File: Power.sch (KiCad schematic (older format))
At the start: 13 parts, among them P1 24 Pin MiniFit JR, SW1 Power Switch

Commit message: Layout Work Session 5
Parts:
- added TP1: CONN_1, symbol CONN_1
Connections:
- net GND: now also TP1.1
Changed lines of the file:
@@
-EESchema Schematic File Version 2  date 11/7/2013 10:50:27 PM
+EESchema Schematic File Version 2  date 11/9/2013 9:10:12 PM
 LIBS:power
 LIBS:device
@@
 Sheet 9 9
 Title ""
-Date "8 nov 2013"
+Date "10 nov 2013"
 Rev ""
 Comp ""
@@
 $EndComp
 $Comp
-L GND #PWR048
+L GND #PWR045
 U 1 1 523DFA76
 P 1400 1850
-F 0 "#PWR048" H 1400 1850 30  0001 C CNN
+F 0 "#PWR045" H 1400 1850 30  0001 C CNN
 F 1 "GND" H 1400 1780 30  0001 C CNN
 F 2 "" H 1400 1850 60  0000 C CNN
@@
 	5500 1900 5500 1150
 $Comp
-L +12P #PWR049
+L +12P #PWR046
 U 1 1 523DFB91
 P 5500 1150
-F 0 "#PWR049" H 5500 1120 30  0001 C CNN
+F 0 "#PWR046" H 5500 1120 30  0001 C CNN
 F 1 "+12P" H 5500 1250 30  0000 C CNN
 F 2 "" H 5500 1150 60  0000 C CNN
@@
 $EndComp
 $Comp
-L -12P #PWR050
+L -12P #PWR047
 U 1 1 523E04D8
 P 6100 1150
-F 0 "#PWR050" H 6100 1280 20  0001 C CNN
+F 0 "#PWR047" H 6100 1280 20  0001 C CNN
 F 1 "-12P" H 6100 1250 30  0000 C CNN
 F 2 "" H 6100 1150 60  0000 C CNN
@@
 	4800 3200 4800 3450
 $Comp
-L GND #PWR051
+L GND #PWR048
 U 1 1 523E08C4
 P 4800 3450
-F 0 "#PWR051" H 4800 3450 30  0001 C CNN
+F 0 "#PWR048" H 4800 3450 30  0001 C CNN
 F 1 "GND" H 4800 3380 30  0001 C CNN
 F 2 "" H 4800 3450 60  0000 C CNN
@@
 	5650 3000 5650 2750
 $Comp
-L +3.3V #PWR052
+L +3.3V #PWR049
 U 1 1 523E0910
 P 5650 2750
-F 0 "#PWR052" H 5650 2710 30  0001 C CNN
+F 0 "#PWR049" H 5650 2710 30  0001 C CNN
 F 1 "+3.3V" H 5650 2860 30  0000 C CNN
 F 2 "" H 5650 2750 60  0000 C CNN
@@
 $EndComp
 $Comp
-L +12P #PWR053
+L +12P #PWR050
 U 1 1 523E0C76
 P 8000 2250
-F 0 "#PWR053" H 8000 2220 30  0001 C CNN
+F 0 "#PWR050" H 8000 2220 30  0001 C CNN
 F 1 "+12P" H 8000 2350 30  0000 C CNN
 F 2 "" H 8000 2250 60  0000 C CNN
@@
 $EndComp
 $Comp
-L -12P #PWR054
+L -12P #PWR051
 U 1 1 523E0C7C
 P 8000 3800
-F 0 "#PWR054" H 8000 3930 20  0001 C CNN
+F 0 "#PWR051" H 8000 3930 20  0001 C CNN
 F 1 "-12P" H 8000 3900 30  0000 C CNN
 F 2 "" H 8000 3800 60  0000 C CNN
@@
 $EndComp
 $Comp
-L GND #PWR055
+L GND #PWR052
 U 1 1 523E0C82
 P 9000 3200
-F 0 "#PWR055" H 9000 3200 30  0001 C CNN
+F 0 "#PWR052" H 9000 3200 30  0001 C CNN
 F 1 "GND" H 9000 3130 30  0001 C CNN
 F 2 "" H 9000 3200 60  0000 C CNN
@@
 Connection ~ 9450 3050
 $Comp
-L -12V #PWR056
+L -12V #PWR053
 U 1 1 523E0DD3
 P 10350 3800
-F 0 "#PWR056" H 10350 3930 20  0001 C CNN
+F 0 "#PWR053" H 10350 3930 20  0001 C CNN
 F 1 "-12V" H 10350 3900 30  0000 C CNN
 F 2 "" H 10350 3800 60  0000 C CNN
@@
 Connection ~ 9450 2450
 $Comp
-L +12V #PWR057
+L +12V #PWR054
 U 1 1 523E0E37
 P 10350 2200
-F 0 "#PWR057" H 10350 2150 20  0001 C CNN
+F 0 "#PWR054" H 10350 2150 20  0001 C CNN
 F 1 "+12V" H 10350 2300 30  0000 C CNN
 F 2 "" H 10350 2200 60  0000 C CNN
@@
 Connection ~ 3450 1900
 $Comp
-L +12C #PWR058
+L +12C #PWR055
 U 1 1 52438F0D
 P 3450 1150
-F 0 "#PWR058" H 3450 1120 30  0001 C CNN
+F 0 "#PWR055" H 3450 1120 30  0001 C CNN
 F 1 "+12C" H 3450 1260 40  0000 C CNN
 F 2 "~" H 3450 1150 60  0000 C CNN
@@
 $EndComp
 $Comp
-L GND #PWR059
+L GND #PWR056
 U 1 1 524502FC
 P 9400 1650
-F 0 "#PWR059" H 9400 1650 30  0001 C CNN
+F 0 "#PWR056" H 9400 1650 30  0001 C CNN
 F 1 "GND" H 9400 1580 30  0001 C CNN
 F 2 "" H 9400 1650 60  0000 C CNN
@@
 $EndComp
 $Comp
-L +5V #PWR060
+L +5V #PWR057
 U 1 1 524503B6
 P 10300 650
-F 0 "#PWR060" H 10300 740 20  0001 C CNN
+F 0 "#PWR057" H 10300 740 20  0001 C CNN
 F 1 "+5V" H 10300 740 30  0000 C CNN
 F 2 "~" H 10300 650 60  0000 C CNN
@@
 $EndComp
 $Comp
-L +3.3V #PWR061
+L +3.3V #PWR058
 U 1 1 526E168C
 P 4400 1150
-F 0 "#PWR061" H 4400 1110 30  0001 C CNN
+F 0 "#PWR058" H 4400 1110 30  0001 C CNN
 F 1 "+3.3V" H 4400 1260 30  0000 C CNN
 F 2 "" H 4400 1150 60  0000 C CNN
@@
 	3550 2000 3550 1500
 Connection ~ 3550 1500
+$Comp
+L CONN_1 TP1
+U 1 1 527EFE16
+P 6650 4050
+F 0 "TP1" H 6730 4050 40  0000 L CNN
+F 1 "CONN_1" H 6650 4105 30  0001 C CNN
+F 2 "" H 6650 4050 60  0000 C CNN
+F 3 "" H 6650 4050 60  0000 C CNN
+	1    6650 4050
+	-1   0    0    1
+$EndComp
+$Comp
+L GND #PWR?
+U 1 1 527EFE6B
+P 6950 4200
+F 0 "#PWR?" H 6950 4200 30  0001 C CNN
+F 1 "GND" H 6950 4130 30  0001 C CNN
+F 2 "" H 6950 4200 60  0000 C CNN
+F 3 "" H 6950 4200 60  0000 C CNN
+	1    6950 4200
+	1    0    0    -1
+$EndComp
+Wire Wire Line
+	6950 4200 6950 4050
+Wire Wire Line
+	6950 4050 6800 4050
 $EndSCHEMATC

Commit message: Layout Work Session 6 Output
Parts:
- added JP1, JP2, JP3, JP4: JUMPER, ~, symbol JUMPER
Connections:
- net GND: now also JP1.1, JP2.1, JP3.1, JP4.1
- new net AGND: JP1.2
- new net GND_LED: JP3.2
- new net GND_PWR: JP2.2
- new net GND_RELAY: JP4.2
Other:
- note added: "Star Point"
- moved on the sheet: TP1
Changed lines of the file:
@@
-EESchema Schematic File Version 2  date 11/9/2013 9:10:12 PM
+EESchema Schematic File Version 2  date 11/10/2013 9:27:17 PM
 LIBS:power
 LIBS:device
@@
 Sheet 9 9
 Title ""
-Date "10 nov 2013"
+Date "11 nov 2013"
 Rev ""
 Comp ""
@@
 $EndComp
 $Comp
-L GND #PWR045
+L GND #PWR51
 U 1 1 523DFA76
 P 1400 1850
-F 0 "#PWR045" H 1400 1850 30  0001 C CNN
+F 0 "#PWR51" H 1400 1850 30  0001 C CNN
 F 1 "GND" H 1400 1780 30  0001 C CNN
 F 2 "" H 1400 1850 60  0000 C CNN
@@
 	5500 1900 5500 1150
 $Comp
-L +12P #PWR046
+L +12P #PWR57
 U 1 1 523DFB91
 P 5500 1150
-F 0 "#PWR046" H 5500 1120 30  0001 C CNN
+F 0 "#PWR57" H 5500 1120 30  0001 C CNN
 F 1 "+12P" H 5500 1250 30  0000 C CNN
 F 2 "" H 5500 1150 60  0000 C CNN
@@
 $EndComp
 $Comp
-L -12P #PWR047
+L -12P #PWR59
 U 1 1 523E04D8
 P 6100 1150
-F 0 "#PWR047" H 6100 1280 20  0001 C CNN
+F 0 "#PWR59" H 6100 1280 20  0001 C CNN
 F 1 "-12P" H 6100 1250 30  0000 C CNN
 F 2 "" H 6100 1150 60  0000 C CNN
@@
 	4800 3200 4800 3450
 $Comp
-L GND #PWR048
+L GND #PWR54
 U 1 1 523E08C4
 P 4800 3450
-F 0 "#PWR048" H 4800 3450 30  0001 C CNN
+F 0 "#PWR54" H 4800 3450 30  0001 C CNN
 F 1 "GND" H 4800 3380 30  0001 C CNN
 F 2 "" H 4800 3450 60  0000 C CNN
@@
 	5650 3000 5650 2750
 $Comp
-L +3.3V #PWR049
+L +3.3V #PWR58
 U 1 1 523E0910
 P 5650 2750
-F 0 "#PWR049" H 5650 2710 30  0001 C CNN
+F 0 "#PWR58" H 5650 2710 30  0001 C CNN
 F 1 "+3.3V" H 5650 2860 30  0000 C CNN
 F 2 "" H 5650 2750 60  0000 C CNN
@@
 $EndComp
 $Comp
-L +12P #PWR050
+L +12P #PWR66
 U 1 1 523E0C76
 P 8000 2250
-F 0 "#PWR050" H 8000 2220 30  0001 C CNN
+F 0 "#PWR66" H 8000 2220 30  0001 C CNN
 F 1 "+12P" H 8000 2350 30  0000 C CNN
 F 2 "" H 8000 2250 60  0000 C CNN
@@
 $EndComp
 $Comp
-L -12P #PWR051
+L -12P #PWR67
 U 1 1 523E0C7C
 P 8000 3800
-F 0 "#PWR051" H 8000 3930 20  0001 C CNN
+F 0 "#PWR67" H 8000 3930 20  0001 C CNN
 F 1 "-12P" H 8000 3900 30  0000 C CNN
 F 2 "" H 8000 3800 60  0000 C CNN
@@
 $EndComp
 $Comp
-L GND #PWR052
+L GND #PWR68
 U 1 1 523E0C82
 P 9000 3200
-F 0 "#PWR052" H 9000 3200 30  0001 C CNN
+F 0 "#PWR68" H 9000 3200 30  0001 C CNN
 F 1 "GND" H 9000 3130 30  0001 C CNN
 F 2 "" H 9000 3200 60  0000 C CNN
@@
 Connection ~ 9450 3050
 $Comp
-L -12V #PWR053
+L -12V #PWR72
 U 1 1 523E0DD3
 P 10350 3800
-F 0 "#PWR053" H 10350 3930 20  0001 C CNN
+F 0 "#PWR72" H 10350 3930 20  0001 C CNN
 F 1 "-12V" H 10350 3900 30  0000 C CNN
 F 2 "" H 10350 3800 60  0000 C CNN
@@
 Connection ~ 9450 2450
 $Comp
-L +12V #PWR054
+L +12V #PWR71
 U 1 1 523E0E37
 P 10350 2200
-F 0 "#PWR054" H 10350 2150 20  0001 C CNN
+F 0 "#PWR71" H 10350 2150 20  0001 C CNN
 F 1 "+12V" H 10350 2300 30  0000 C CNN
 F 2 "" H 10350 2200 60  0000 C CNN
@@
 Connection ~ 3450 1900
 $Comp
-L +12C #PWR055
+L +12C #PWR52
 U 1 1 52438F0D
 P 3450 1150
-F 0 "#PWR055" H 3450 1120 30  0001 C CNN
+F 0 "#PWR52" H 3450 1120 30  0001 C CNN
 F 1 "+12C" H 3450 1260 40  0000 C CNN
 F 2 "~" H 3450 1150 60  0000 C CNN
@@
 $EndComp
 $Comp
-L GND #PWR056
+L GND #PWR69
 U 1 1 524502FC
 P 9400 1650
-F 0 "#PWR056" H 9400 1650 30  0001 C CNN
+F 0 "#PWR69" H 9400 1650 30  0001 C CNN
 F 1 "GND" H 9400 1580 30  0001 C CNN
 F 2 "" H 9400 1650 60  0000 C CNN
@@
 Connection ~ 9400 900
 $Comp
-L +5P #PWR58
+L +5P #PWR56
 U 1 1 52450355
 P 4900 1150
-F 0 "#PWR58" H 4900 1280 20  0001 C CNN
+F 0 "#PWR56" H 4900 1280 20  0001 C CNN
 F 1 "+5P" H 4900 1250 30  0000 C CNN
 F 2 "~" H 4900 1150 60  0000 C CNN
@@
 $EndComp
 $Comp
-L +5P #PWR62
+L +5P #PWR65
 U 1 1 52450371
 P 7950 700
-F 0 "#PWR62" H 7950 830 20  0001 C CNN
+F 0 "#PWR65" H 7950 830 20  0001 C CNN
 F 1 "+5P" H 7950 800 30  0000 C CNN
 F 2 "~" H 7950 700 60  0000 C CNN
@@
 $EndComp
 $Comp
-L +5V #PWR057
+L +5V #PWR70
 U 1 1 524503B6
 P 10300 650
-F 0 "#PWR057" H 10300 740 20  0001 C CNN
+F 0 "#PWR70" H 10300 740 20  0001 C CNN
 F 1 "+5V" H 10300 740 30  0000 C CNN
 F 2 "~" H 10300 650 60  0000 C CNN
@@
 $EndComp
 $Comp
-L +3.3V #PWR058
+L +3.3V #PWR53
 U 1 1 526E168C
 P 4400 1150
-F 0 "#PWR058" H 4400 1110 30  0001 C CNN
+F 0 "#PWR53" H 4400 1110 30  0001 C CNN
 F 1 "+3.3V" H 4400 1260 30  0000 C CNN
 F 2 "" H 4400 1150 60  0000 C CNN
@@
 L CONN_1 TP1
 U 1 1 527EFE16
-P 6650 4050
-F 0 "TP1" H 6730 4050 40  0000 L CNN
-F 1 "CONN_1" H 6650 4105 30  0001 C CNN
-F 2 "" H 6650 4050 60  0000 C CNN
-F 3 "" H 6650 4050 60  0000 C CNN
-	1    6650 4050
+P 5800 5400
+F 0 "TP1" H 5880 5400 40  0000 L CNN
+F 1 "CONN_1" H 5800 5455 30  0001 C CNN
+F 2 "" H 5800 5400 60  0000 C CNN
+F 3 "" H 5800 5400 60  0000 C CNN
+	1    5800 5400
 	-1   0    0    1
 $EndComp
 $Comp
-L GND #PWR?
+L GND #PWR60
 U 1 1 527EFE6B
-P 6950 4200
-F 0 "#PWR?" H 6950 4200 30  0001 C CNN
-F 1 "GND" H 6950 4130 30  0001 C CNN
-F 2 "" H 6950 4200 60  0000 C CNN
-F 3 "" H 6950 4200 60  0000 C CNN
-	1    6950 4200
-	1    0    0    -1
-$EndComp
-Wire Wire Line
-	6950 4200 6950 4050
-Wire Wire Line
-	6950 4050 6800 4050
+P 6100 5550
+F 0 "#PWR60" H 6100 5550 30  0001 C CNN
+F 1 "GND" H 6100 5480 30  0001 C CNN
+F 2 "" H 6100 5550 60  0000 C CNN
+F 3 "" H 6100 5550 60  0000 C CNN
+	1    6100 5550
+	1    0    0    -1
+$EndComp
+Wire Wire Line
+	6100 5550 6100 5400
+Wire Wire Line
+	6100 5400 5950 5400
+Text Notes 5100 5400 0    60   ~ 0
+Star Point
+$Comp
+L JUMPER JP1
+U 1 1 52804A88
+P 5450 6050
+F 0 "JP1" H 5450 6200 60  0000 C CNN
+F 1 "JUMPER" H 5450 5970 40  0000 C CNN
+F 2 "~" H 5450 6050 60  0000 C CNN
+F 3 "~" H 5450 6050 60  0000 C CNN
+	1    5450 6050
+	1    0    0    -1
+$EndComp
+$Comp
+L JUMPER JP2
+U 1 1 52804A95
+P 5450 6450
+F 0 "JP2" H 5450 6600 60  0000 C CNN
+F 1 "JUMPER" H 5450 6370 40  0000 C CNN
+F 2 "~" H 5450 6450 60  0000 C CNN
+F 3 "~" H 5450 6450 60  0000 C CNN
+	1    5450 6450
+	1    0    0    -1
+$EndComp
+$Comp
+L JUMPER JP3
+U 1 1 52804A9B
+P 5450 6800
+F 0 "JP3" H 5450 6950 60  0000 C CNN
+F 1 "JUMPER" H 5450 6720 40  0000 C CNN
+F 2 "~" H 5450 6800 60  0000 C CNN
+F 3 "~" H 5450 6800 60  0000 C CNN
+	1    5450 6800
+	1    0    0    -1
+$EndComp
+$Comp
+L JUMPER JP4
+U 1 1 52804AA1
+P 5450 7150
+F 0 "JP4" H 5450 7300 60  0000 C CNN
+F 1 "JUMPER" H 5450 7070 40  0000 C CNN
+F 2 "~" H 5450 7150 60  0000 C CNN
+F 3 "~" H 5450 7150 60  0000 C CNN
+	1    5450 7150
+	1    0    0    -1
+$EndComp
+$Comp
+L GND #PWR55
+U 1 1 52804AA7
+P 4800 7450
+F 0 "#PWR55" H 4800 7450 30  0001 C CNN
+F 1 "GND" H 4800 7380 30  0001 C CNN
+F 2 "" H 4800 7450 60  0000 C CNN
+F 3 "" H 4800 7450 60  0000 C CNN
+	1    4800 7450
+	1    0    0    -1
+$EndComp
+Wire Wire Line
+	4800 7450 4800 6050
+Wire Wire Line
+	4800 6050 5150 6050
+Wire Wire Line
+	4800 6450 5150 6450
+Connection ~ 4800 6450
+Wire Wire Line
+	5150 6800 4800 6800
+Connection ~ 4800 6800
+Wire Wire Line
+	5150 7150 4800 7150
+Connection ~ 4800 7150
+Wire Wire Line
+	5750 6050 6200 6050
+$Comp
+L GND_RELAY #PWR64
+U 1 1 52804C2C
+P 6200 7400
+F 0 "#PWR64" H 6200 7400 30  0001 C CNN
+F 1 "GND_RELAY" H 6200 7330 30  0000 C CNN
+F 2 "~" H 6200 7400 60  0000 C CNN
+F 3 "~" H 6200 7400 60  0000 C CNN
+	1    6200 7400
+	1    0    0    -1
+$EndComp
+$Comp
+L GND_LED #PWR63
+U 1 1 52804C3B
+P 6200 6950
+F 0 "#PWR63" H 6200 6950 30  0001 C CNN
+F 1 "GND_LED" H 6200 6880 30  0000 C CNN
+F 2 "~" H 6200 6950 60  0000 C CNN
+F 3 "~" H 6200 6950 60  0000 C CNN
+	1    6200 6950
+	1    0    0    -1
+$EndComp
+$Comp
+L GND_PWR #PWR62
+U 1 1 52804C4A
+P 6200 6550
+F 0 "#PWR62" H 6200 6550 30  0001 C CNN
+F 1 "GND_PWR" H 6200 6480 30  0000 C CNN
+F 2 "~" H 6200 6550 60  0000 C CNN
+F 3 "~" H 6200 6550 60  0000 C CNN
+	1    6200 6550
+	1    0    0    -1
+$EndComp
+$Comp
+L AGND #PWR61
+U 1 1 52804C59
+P 6200 6200
+F 0 "#PWR61" H 6200 6200 40  0001 C CNN
+F 1 "AGND" H 6200 6130 50  0000 C CNN
+F 2 "~" H 6200 6200 60  0000 C CNN
+F 3 "~" H 6200 6200 60  0000 C CNN
+	1    6200 6200
+	1    0    0    -1
+$EndComp
+Wire Wire Line
+	6200 6050 6200 6200
+Wire Wire Line
+	6200 6550 6200 6450
+Wire Wire Line
+	6200 6450 5750 6450
+Wire Wire Line
+	5750 6800 6200 6800
+Wire Wire Line
+	6200 6800 6200 6950
+Wire Wire Line
+	6200 7400 6200 7150
+Wire Wire Line
+	6200 7150 5750 7150
 $EndSCHEMATC

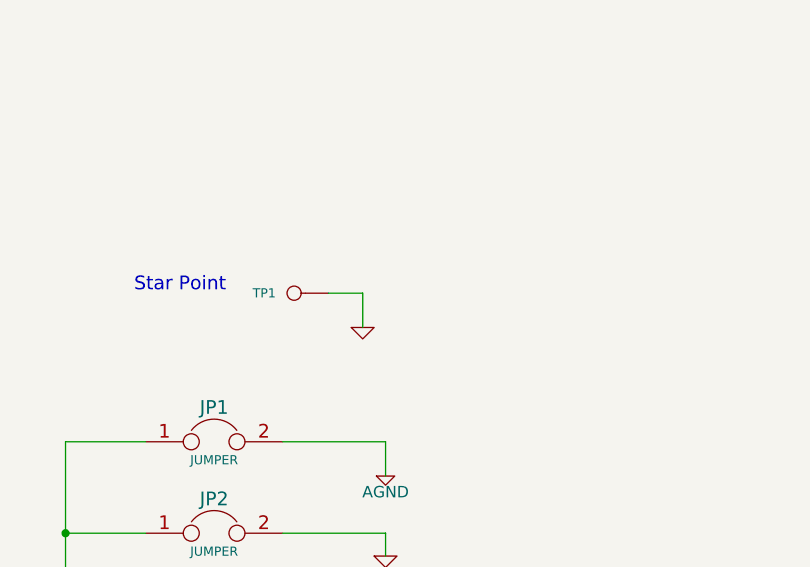
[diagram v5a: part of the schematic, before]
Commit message: Connecting Grounds Together
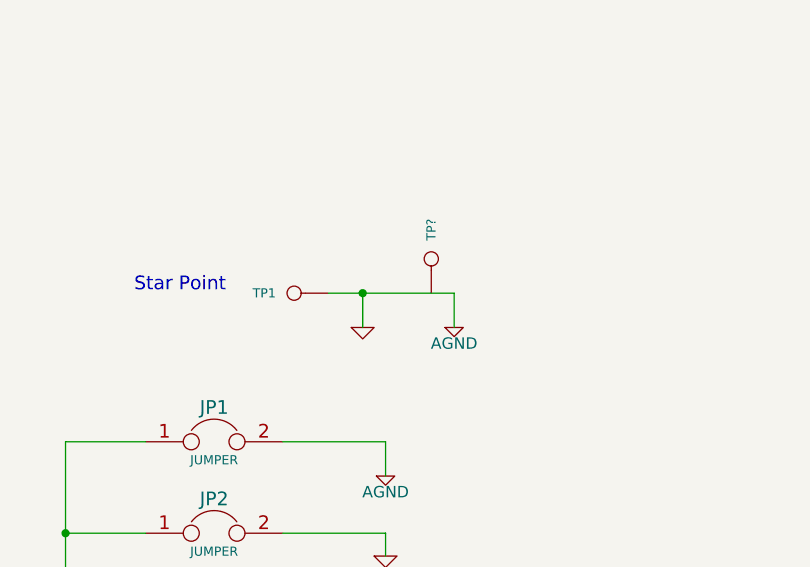
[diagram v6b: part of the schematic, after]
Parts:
- added TP?: CONN_1, symbol CONN_1
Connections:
- net GND is gone; now on net AGND: C2.2, C3.2, C4.1, JP1.1, JP2.1, JP3.1, JP4.1, P1.3 (P3), P1.5 (P5), SW1.3, TP1.1
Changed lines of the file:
@@
-EESchema Schematic File Version 2  date 11/13/2013 1:25:48 AM
+EESchema Schematic File Version 2  date 11/13/2013 11:53:23 PM
 LIBS:power
 LIBS:device
@@
 Sheet 9 9
 Title ""
-Date "13 nov 2013"
+Date "14 nov 2013"
 Rev ""
 Comp ""
@@
 $EndComp
 $Comp
-L GND #PWR51
+L GND #PWR044
 U 1 1 523DFA76
 P 1400 1850
-F 0 "#PWR51" H 1400 1850 30  0001 C CNN
+F 0 "#PWR044" H 1400 1850 30  0001 C CNN
 F 1 "GND" H 1400 1780 30  0001 C CNN
 F 2 "" H 1400 1850 60  0000 C CNN
@@
 	5500 1900 5500 1150
 $Comp
-L +12P #PWR57
+L +12P #PWR045
 U 1 1 523DFB91
 P 5500 1150
-F 0 "#PWR57" H 5500 1120 30  0001 C CNN
+F 0 "#PWR045" H 5500 1120 30  0001 C CNN
 F 1 "+12P" H 5500 1250 30  0000 C CNN
 F 2 "" H 5500 1150 60  0000 C CNN
@@
 $EndComp
 $Comp
-L -12P #PWR59
+L -12P #PWR046
 U 1 1 523E04D8
 P 6100 1150
-F 0 "#PWR59" H 6100 1280 20  0001 C CNN
+F 0 "#PWR046" H 6100 1280 20  0001 C CNN
 F 1 "-12P" H 6100 1250 30  0000 C CNN
 F 2 "" H 6100 1150 60  0000 C CNN
@@
 	4800 3200 4800 3450
 $Comp
-L GND #PWR54
+L GND #PWR047
 U 1 1 523E08C4
 P 4800 3450
-F 0 "#PWR54" H 4800 3450 30  0001 C CNN
+F 0 "#PWR047" H 4800 3450 30  0001 C CNN
 F 1 "GND" H 4800 3380 30  0001 C CNN
 F 2 "" H 4800 3450 60  0000 C CNN
@@
 	5650 3000 5650 2750
 $Comp
-L +3.3V #PWR58
+L +3.3V #PWR048
 U 1 1 523E0910
 P 5650 2750
-F 0 "#PWR58" H 5650 2710 30  0001 C CNN
+F 0 "#PWR048" H 5650 2710 30  0001 C CNN
 F 1 "+3.3V" H 5650 2860 30  0000 C CNN
 F 2 "" H 5650 2750 60  0000 C CNN
@@
 $EndComp
 $Comp
-L +12P #PWR66
+L +12P #PWR049
 U 1 1 523E0C76
 P 8000 2250
-F 0 "#PWR66" H 8000 2220 30  0001 C CNN
+F 0 "#PWR049" H 8000 2220 30  0001 C CNN
 F 1 "+12P" H 8000 2350 30  0000 C CNN
 F 2 "" H 8000 2250 60  0000 C CNN
@@
 $EndComp
 $Comp
-L -12P #PWR67
+L -12P #PWR050
 U 1 1 523E0C7C
 P 8000 3800
-F 0 "#PWR67" H 8000 3930 20  0001 C CNN
+F 0 "#PWR050" H 8000 3930 20  0001 C CNN
 F 1 "-12P" H 8000 3900 30  0000 C CNN
 F 2 "" H 8000 3800 60  0000 C CNN
@@
 $EndComp
 $Comp
-L GND #PWR68
+L GND #PWR051
 U 1 1 523E0C82
 P 9000 3200
-F 0 "#PWR68" H 9000 3200 30  0001 C CNN
+F 0 "#PWR051" H 9000 3200 30  0001 C CNN
 F 1 "GND" H 9000 3130 30  0001 C CNN
 F 2 "" H 9000 3200 60  0000 C CNN
@@
 Connection ~ 9450 3050
 $Comp
-L -12V #PWR72
+L -12V #PWR052
 U 1 1 523E0DD3
 P 10350 3800
-F 0 "#PWR72" H 10350 3930 20  0001 C CNN
+F 0 "#PWR052" H 10350 3930 20  0001 C CNN
 F 1 "-12V" H 10350 3900 30  0000 C CNN
 F 2 "" H 10350 3800 60  0000 C CNN
@@
 Connection ~ 9450 2450
 $Comp
-L +12V #PWR71
+L +12V #PWR053
 U 1 1 523E0E37
 P 10350 2200
-F 0 "#PWR71" H 10350 2150 20  0001 C CNN
+F 0 "#PWR053" H 10350 2150 20  0001 C CNN
 F 1 "+12V" H 10350 2300 30  0000 C CNN
 F 2 "" H 10350 2200 60  0000 C CNN
@@
 Connection ~ 3450 1900
 $Comp
-L +12C #PWR52
+L +12C #PWR054
 U 1 1 52438F0D
 P 3450 1150
-F 0 "#PWR52" H 3450 1120 30  0001 C CNN
+F 0 "#PWR054" H 3450 1120 30  0001 C CNN
 F 1 "+12C" H 3450 1260 40  0000 C CNN
 F 2 "~" H 3450 1150 60  0000 C CNN
@@
 $EndComp
 $Comp
-L GND #PWR69
+L GND #PWR055
 U 1 1 524502FC
 P 9400 1650
-F 0 "#PWR69" H 9400 1650 30  0001 C CNN
+F 0 "#PWR055" H 9400 1650 30  0001 C CNN
 F 1 "GND" H 9400 1580 30  0001 C CNN
 F 2 "" H 9400 1650 60  0000 C CNN
@@
 $EndComp
 $Comp
-L +5V #PWR70
+L +5V #PWR056
 U 1 1 524503B6
 P 10300 650
-F 0 "#PWR70" H 10300 740 20  0001 C CNN
+F 0 "#PWR056" H 10300 740 20  0001 C CNN
 F 1 "+5V" H 10300 740 30  0000 C CNN
 F 2 "~" H 10300 650 60  0000 C CNN
@@
 $EndComp
 $Comp
-L +3.3V #PWR53
+L +3.3V #PWR057
 U 1 1 526E168C
 P 4400 1150
-F 0 "#PWR53" H 4400 1110 30  0001 C CNN
+F 0 "#PWR057" H 4400 1110 30  0001 C CNN
 F 1 "+3.3V" H 4400 1260 30  0000 C CNN
 F 2 "" H 4400 1150 60  0000 C CNN
@@
 $EndComp
 $Comp
-L GND #PWR60
+L GND #PWR058
 U 1 1 527EFE6B
 P 6100 5550
-F 0 "#PWR60" H 6100 5550 30  0001 C CNN
+F 0 "#PWR058" H 6100 5550 30  0001 C CNN
 F 1 "GND" H 6100 5480 30  0001 C CNN
 F 2 "" H 6100 5550 60  0000 C CNN
@@
 	6100 5550 6100 5400
 Wire Wire Line
-	6100 5400 5950 5400
+	5950 5400 6500 5400
 Text Notes 5100 5400 0    60   ~ 0
 Star Point
@@
 $EndComp
 $Comp
-L GND #PWR55
+L GND #PWR059
 U 1 1 52804AA7
 P 4800 7450
-F 0 "#PWR55" H 4800 7450 30  0001 C CNN
+F 0 "#PWR059" H 4800 7450 30  0001 C CNN
 F 1 "GND" H 4800 7380 30  0001 C CNN
 F 2 "" H 4800 7450 60  0000 C CNN
@@
 	5750 6050 6200 6050
 $Comp
-L GND_RELAY #PWR64
+L GND_RELAY #PWR060
 U 1 1 52804C2C
 P 6200 7400
-F 0 "#PWR64" H 6200 7400 30  0001 C CNN
+F 0 "#PWR060" H 6200 7400 30  0001 C CNN
 F 1 "GND_RELAY" H 6200 7330 30  0000 C CNN
 F 2 "~" H 6200 7400 60  0000 C CNN
@@
 $EndComp
 $Comp
-L GND_LED #PWR63
+L GND_LED #PWR061
 U 1 1 52804C3B
 P 6200 6950
-F 0 "#PWR63" H 6200 6950 30  0001 C CNN
+F 0 "#PWR061" H 6200 6950 30  0001 C CNN
 F 1 "GND_LED" H 6200 6880 30  0000 C CNN
 F 2 "~" H 6200 6950 60  0000 C CNN
@@
 $EndComp
 $Comp
-L GND_PWR #PWR62
+L GND_PWR #PWR062
 U 1 1 52804C4A
 P 6200 6550
-F 0 "#PWR62" H 6200 6550 30  0001 C CNN
+F 0 "#PWR062" H 6200 6550 30  0001 C CNN
 F 1 "GND_PWR" H 6200 6480 30  0000 C CNN
 F 2 "~" H 6200 6550 60  0000 C CNN
@@
 $EndComp
 $Comp
-L AGND #PWR61
+L AGND #PWR063
 U 1 1 52804C59
 P 6200 6200
-F 0 "#PWR61" H 6200 6200 40  0001 C CNN
+F 0 "#PWR063" H 6200 6200 40  0001 C CNN
 F 1 "AGND" H 6200 6130 50  0000 C CNN
 F 2 "~" H 6200 6200 60  0000 C CNN
@@
 Wire Wire Line
 	6200 7150 5750 7150
+$Comp
+L AGND #PWR064
+U 1 1 5284640B
+P 6500 5550
+F 0 "#PWR064" H 6500 5550 40  0001 C CNN
+F 1 "AGND" H 6500 5480 50  0000 C CNN
+F 2 "~" H 6500 5550 60  0000 C CNN
+F 3 "~" H 6500 5550 60  0000 C CNN
+	1    6500 5550
+	1    0    0    -1
+$EndComp
+Wire Wire Line
+	6500 5400 6500 5550
+Connection ~ 6100 5400
+$Comp
+L CONN_1 TP?
+U 1 1 52846001
+P 6400 5250
+F 0 "TP?" H 6480 5250 40  0000 L CNN
+F 1 "CONN_1" H 6400 5305 30  0001 C CNN
+F 2 "" H 6400 5250 60  0000 C CNN
+F 3 "" H 6400 5250 60  0000 C CNN
+	1    6400 5250
+	0    -1   -1   0
+$EndComp
 $EndSCHEMATC
